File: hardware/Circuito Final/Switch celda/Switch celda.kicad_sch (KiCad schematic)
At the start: 17 parts, among them Q1 MMBT2222A, Q2 MMBT2907A, Q3 MMBT2222A

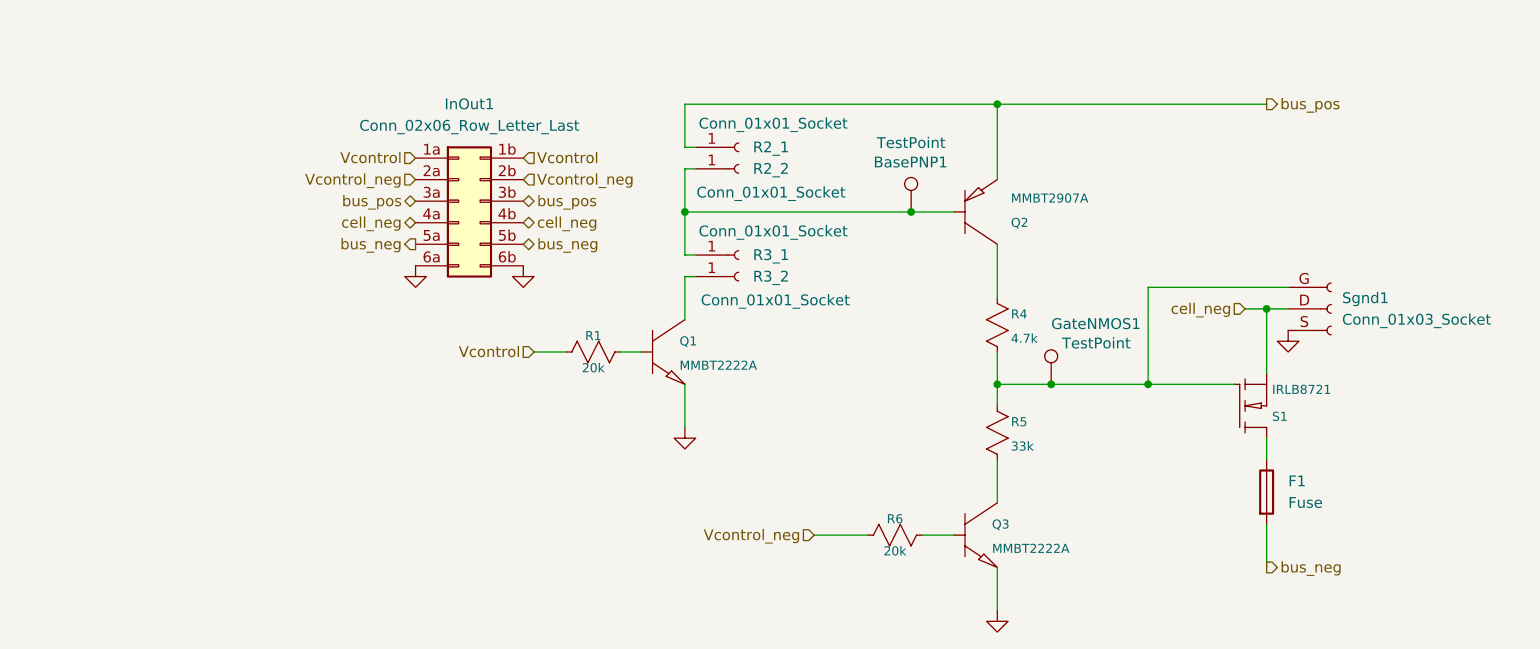
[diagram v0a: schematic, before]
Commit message: Proyecto de la celda corregido
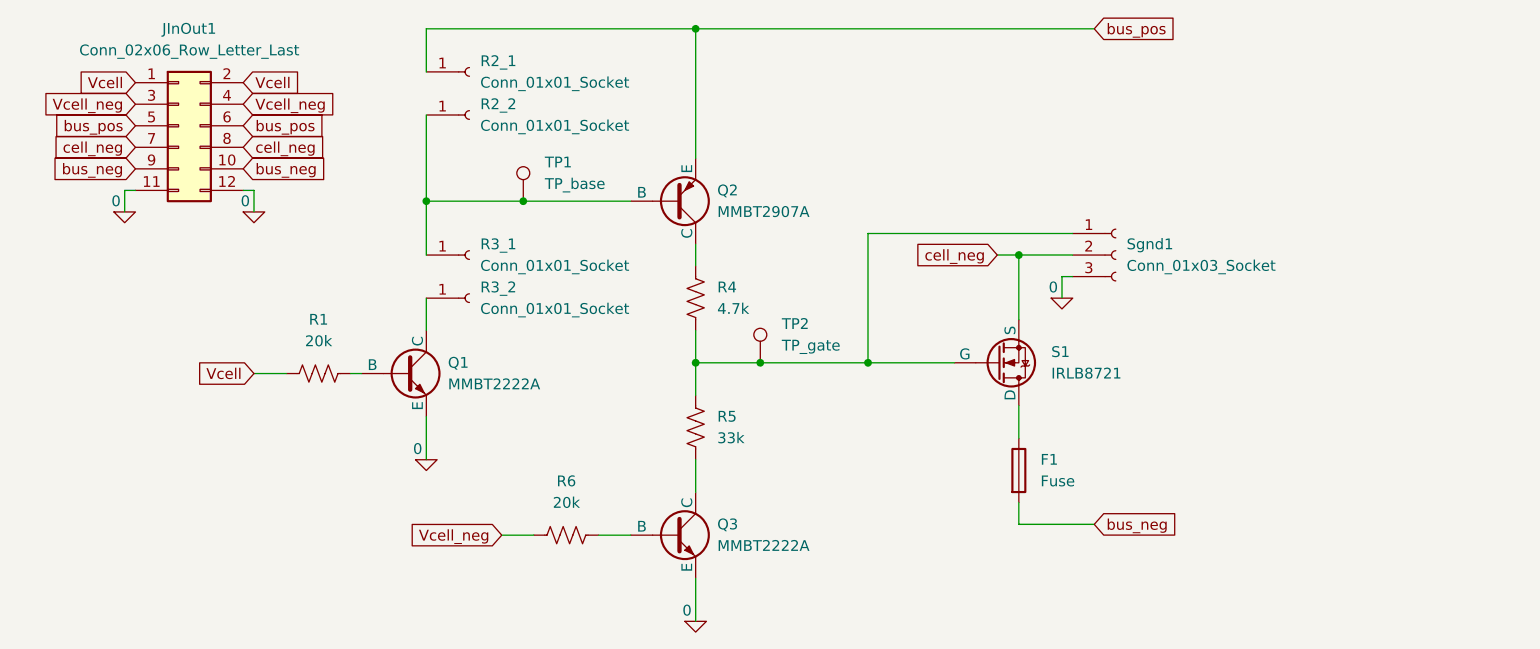
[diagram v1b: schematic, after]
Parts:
- removed BasePNP1, GateNMOS1: TestPoint, TestPoint:TestPoint_Bridge_Pitch2.54mm_Drill1.0mm, symbol Connector:TestPoint
- removed InOut1: Conn_02x06_Row_Letter_Last, Connector_PinHeader_2.54mm:PinHeader_2x06_P2.54mm_Vertical, symbol Connector_Generic:Conn_02x06_Row_Letter_Last
- removed Q1, Q3: MMBT2222A, Package_TO_SOT_SMD:SOT-23-3, symbol modificados:npn
- removed Q2: MMBT2907A, Package_TO_SOT_SMD:SOT-23-3, symbol modificados:pnp
- removed R1, R6: 20k, Resistor_THT:R_Axial_DIN0207_L6.3mm_D2.5mm_P7.62mm_Horizontal, symbol ltspice:res
- removed R4: 4.7k, Resistor_THT:R_Axial_DIN0207_L6.3mm_D2.5mm_P7.62mm_Horizontal, symbol ltspice:res
- removed R5: 33k, Resistor_THT:R_Axial_DIN0207_L6.3mm_D2.5mm_P7.62mm_Horizontal, symbol ltspice:res
- removed S1: IRLB8721, Package_TO_SOT_THT:TO-220-3_Vertical, symbol modificados:nmos
- added JInOut1: Conn_02x06_Row_Letter_Last, Connector_PinHeader_2.54mm:PinHeader_2x06_P2.54mm_Horizontal, symbol Connector_Generic:Conn_02x06_Row_Letter_Last
- added Q1, Q3: MMBT2222A, Package_TO_SOT_SMD:SOT-23-3, symbol Simulation_SPICE:NPN
- added Q2: MMBT2907A, Package_TO_SOT_SMD:SOT-23-3, symbol Simulation_SPICE:PNP
- added R1, R6: 20k, Resistor_SMD:R_0603_1608Metric_Pad0.98x0.95mm_HandSolder, symbol Device:R_US
- added R4: 4.7k, Resistor_SMD:R_0603_1608Metric_Pad0.98x0.95mm_HandSolder, symbol Device:R_US
- added R5: 33k, Resistor_SMD:R_0603_1608Metric_Pad0.98x0.95mm_HandSolder, symbol Device:R_US
- added S1: IRLB8721, Package_TO_SOT_THT:TO-220-3_Vertical, symbol Simulation_SPICE:NMOS
- added TP1: TP_base, TestPoint:TestPoint_Bridge_Pitch2.54mm_Drill1.0mm, symbol Connector:TestPoint
- added TP2: TP_gate, TestPoint:TestPoint_Bridge_Pitch2.54mm_Drill1.0mm, symbol Connector:TestPoint
- F1: footprint Huellas:Fuseholder_Cylinder-5x20mm_Schurter_0031_8201_Horizontal_Open -> Resistor_SMD:R_0603_1608Metric_Pad0.98x0.95mm_HandSolder
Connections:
- net 0: now also Sgnd1.3 (Pin_3), JInOut1.11 (Pin_6a), JInOut1.12 (Pin_6b), Q1.3 (E), Q3.3 (E); no longer Sgnd1.S (Pin_3)
- net bus_neg: now also JInOut1.10 (Pin_5b), JInOut1.9 (Pin_5a)
- net bus_pos: now also JInOut1.5 (Pin_3a), JInOut1.6 (Pin_3b), Q2.3 (E)
- net cell_neg: now also Sgnd1.2 (Pin_2), JInOut1.7 (Pin_4a), JInOut1.8 (Pin_4b), S1.3 (S); no longer Sgnd1.D (Pin_2)
- net at F1.1: now also S1.1 (D)
- net at R2_2.1 (Pin_1), R3_1.1 (Pin_1): now also Q2.2 (B), TP1.1
- net at R3_2.1 (Pin_1): now also Q1.1 (C)
- new net: R4.1, R5.2, S1.2 (G), Sgnd1.1 (Pin_1), TP2.1
- new net: Q3.1 (C), R5.1
- new net: Q3.2 (B), R6.2
- new net: Q1.2 (B), R1.2
- new net: Q2.1 (C), R4.2
- new net Vcell: JInOut1.1 (Pin_1a), JInOut1.2 (Pin_1b), R1.1
- new net Vcell_neg: JInOut1.3 (Pin_2a), JInOut1.4 (Pin_2b), R6.1

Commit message: sube mediciones y comentarios de kicad
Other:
- note added: "agregar LED agregar micro ATtiny agregar inversor MOS? volar Vcell_neg y agregar Vcc (todas compartidas salvo cell_neg) topologia torrecita por banco"
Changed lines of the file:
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@@
+		)
+	)
+	(text "agregar LED\nagregar micro ATtiny\nagregar inversor MOS?\nvolar Vcell_neg y agregar Vcc (todas compartidas salvo cell_neg)\ntopologia torrecita por banco\n"
+		(exclude_from_sim no)
+		(at 48.26 115.062 0)
+		(effects
+			(font
+				(size 1.27 1.27)
+			)
 		)
 	)

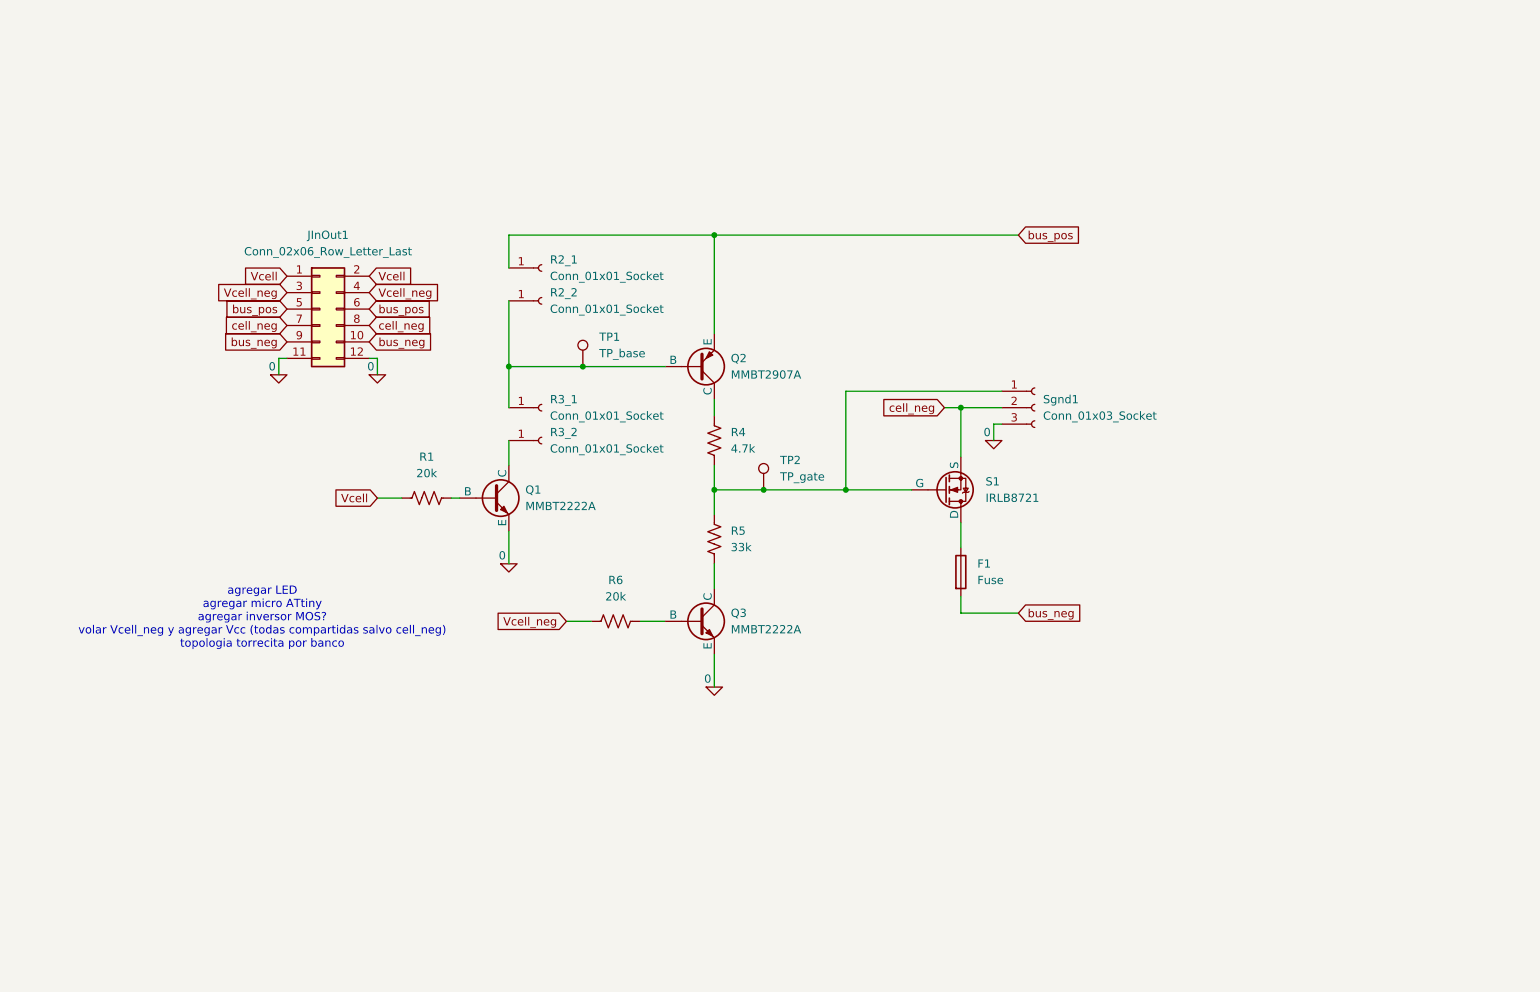
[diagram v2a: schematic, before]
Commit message: Actualización del esqumático del circuito de las celdas
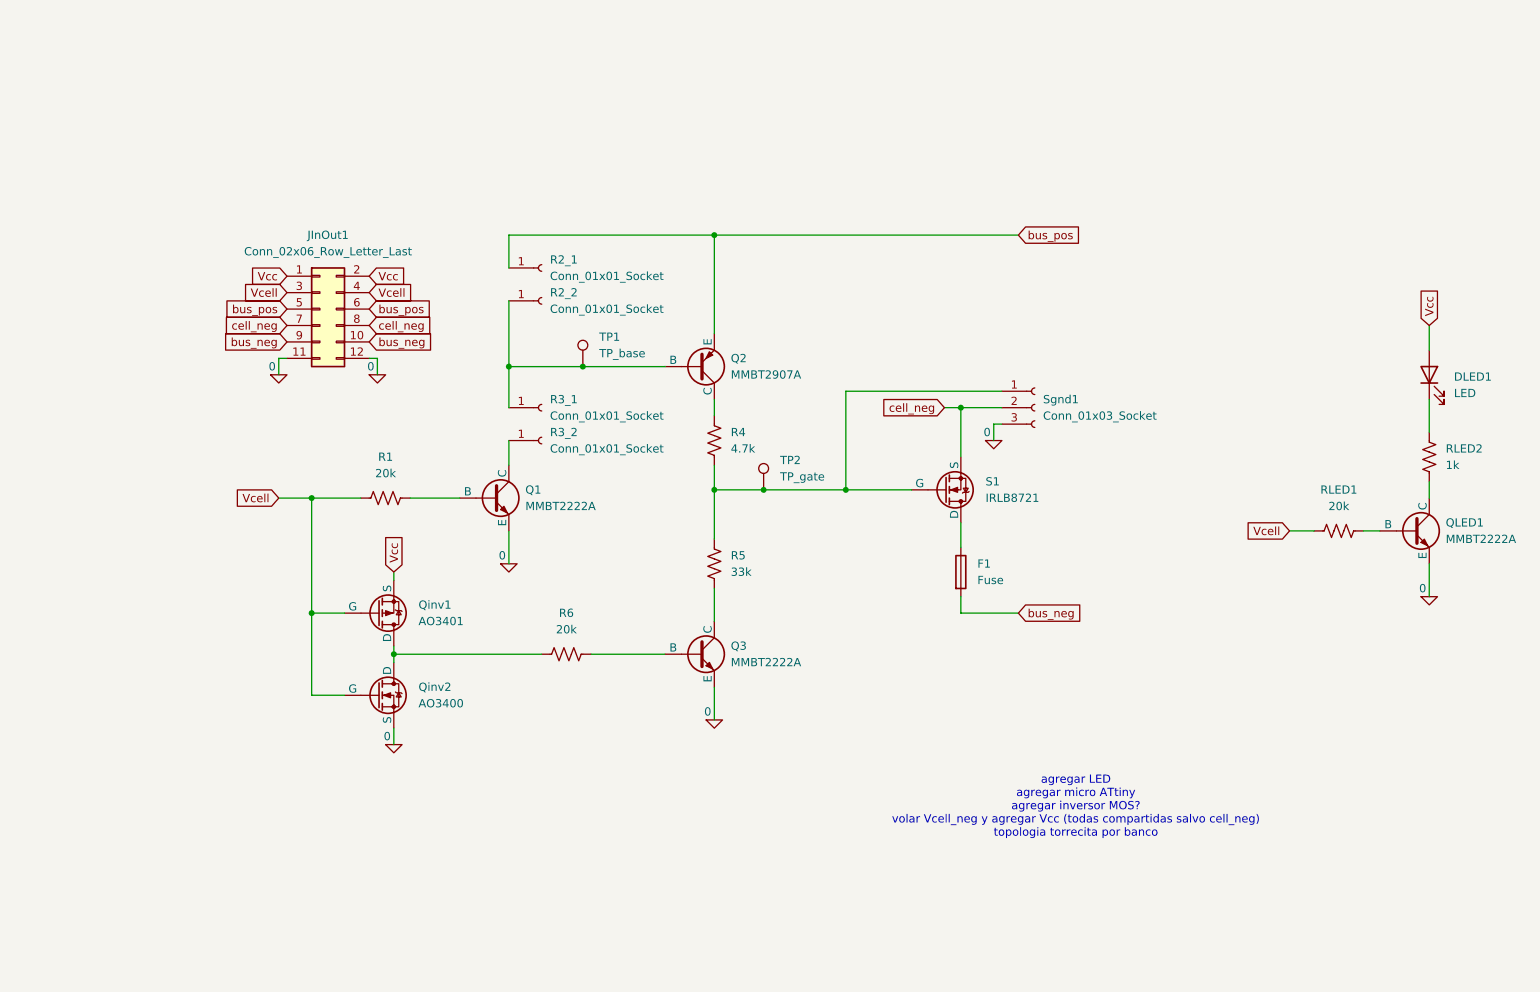
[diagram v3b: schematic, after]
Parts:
- added DLED1: LED, symbol Device:LED
- added QLED1: MMBT2222A, Package_TO_SOT_SMD:SOT-23-3, symbol Simulation_SPICE:NPN
- added Qinv1: AO3401, symbol Simulation_SPICE:PMOS
- added Qinv2: AO3400, symbol Simulation_SPICE:NMOS
- added RLED1: 20k, Resistor_SMD:R_0603_1608Metric_Pad0.98x0.95mm_HandSolder, symbol Device:R_US
- added RLED2: 1k, Resistor_SMD:R_0603_1608Metric_Pad0.98x0.95mm_HandSolder, symbol Device:R_US
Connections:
- net 0: now also QLED1.3 (E), Qinv2.3 (S)
- net Vcell: now also JInOut1.3 (Pin_2a), JInOut1.4 (Pin_2b), Qinv1.2 (G), Qinv2.2 (G), RLED1.1; no longer JInOut1.1 (Pin_1a), JInOut1.2 (Pin_1b)
- removed net Vcell_neg: JInOut1.3 (Pin_2a), JInOut1.4 (Pin_2b), R6.1
- new net: Qinv1.1 (D), Qinv2.1 (D), R6.1
- new net: QLED1.2 (B), RLED1.2
- new net: QLED1.1 (C), RLED2.1
- new net: DLED1.1 (K), RLED2.2
- new net Vcc: DLED1.2 (A), JInOut1.1 (Pin_1a), JInOut1.2 (Pin_1b), Qinv1.3 (S)
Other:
- moved on the sheet: Q3, R1, R5, R6

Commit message: Se elimina el fusible del circuito del switch de las celdas
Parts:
- removed F1: Fuse, Resistor_SMD:R_0603_1608Metric_Pad0.98x0.95mm_HandSolder, symbol Device:Fuse
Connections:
- net bus_neg: now also S1.1 (D)
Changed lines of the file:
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@@
 	(generator_version "9.0")
 	(paper "A4")
-		(symbol "Device:Fuse"
-			(pin_numbers
-				(hide yes)
-			)
-			(pin_names
-				(offset 0)
-			)
-			(exclude_from_sim no)
-			(in_bom yes)
-			(on_board yes)
-			(property "Reference" "F"
-				(at 2.032 0 90)
-				(effects
-					(font
-						(size 1.27 1.27)
-					)
-				)
-			)
-			(property "Value" "Fuse"
-				(at -1.905 0 90)
-				(effects
-					(font
-						(size 1.27 1.27)
-					)
-				)
-			)
-			(property "Footprint" ""
-				(at -1.778 0 90)
-				(effects
-					(font
-						(size 1.27 1.27)
-					)
-					(hide yes)
-				)
-			)
-			(property "Datasheet" "~"
-				(at 0 0 0)
-				(effects
-					(font
-						(size 1.27 1.27)
-					)
-					(hide yes)
-				)
-			)
-			(property "Description" "Fuse"
-				(at 0 0 0)
-				(effects
-					(font
-						(size 1.27 1.27)
-					)
-					(hide yes)
-				)
-			)
-			(property "ki_keywords" "fuse"
-				(at 0 0 0)
-				(effects
-					(font
-						(size 1.27 1.27)
-					)
-					(hide yes)
-				)
-			)
-			(property "ki_fp_filters" "*Fuse*"
-				(at 0 0 0)
-				(effects
-					(font
-						(size 1.27 1.27)
-					)
-					(hide yes)
-				)
-			)
-			(symbol "Fuse_0_1"
-				(rectangle
-					(start -0.762 -2.54)
-					(end 0.762 2.54)
-					(stroke
-						(width 0.254)
-						(type default)
-					)
-					(fill
-						(type none)
-					)
-				)
-				(polyline
-					(pts
-						(xy 0 2.54) (xy 0 -2.54)
-					)
-					(stroke
-						(width 0)
-						(type default)
-					)
-					(fill
-						(type none)
-					)
-				)
-			)
-			(symbol "Fuse_1_1"
-				(pin passive line
-					(at 0 3.81 270)
-					(length 1.27)
-					(name "~"
-						(effects
-							(font
-								(size 1.27 1.27)
-							)
-						)
-					)
-					(number "1"
-						(effects
-							(font
-								(size 1.27 1.27)
-							)
-						)
-					)
-				)
-				(pin passive line
-					(at 0 -3.81 90)
-					(length 1.27)
-					(name "~"
-						(effects
-							(font
-								(size 1.27 1.27)
-							)
-						)
-					)
-					(number "2"
-						(effects
-							(font
-								(size 1.27 1.27)
-							)
-						)
-					)
-				)
-			)
-			(embedded_fonts no)
-		)
 		(symbol "Device:LED"
 			(pin_numbers
@@
 	(wire
 		(pts
-			(xy 156.21 100.33) (xy 156.21 104.14)
-		)
-		(stroke
-			(width 0)
-			(type default)
-		)
-	)
-	(wire
-		(pts
 			(xy 161.29 85.09) (xy 161.29 87.63)
 		)
@@
 	(wire
 		(pts
-			(xy 156.21 114.3) (xy 165.1 114.3)
-		)
-		(stroke
-			(width 0)
-			(type default)
-		)
-	)
-	(wire
-		(pts
 			(xy 228.6 106.68) (xy 228.6 111.76)
 		)
@@
 	(wire
 		(pts
-			(xy 156.21 111.76) (xy 156.21 114.3)
+			(xy 156.21 100.33) (xy 156.21 106.68)
 		)
 		(stroke
@@
 	(global_label "bus_neg"
 		(shape input)
-		(at 165.1 114.3 0)
+		(at 156.21 106.68 270)
 		(fields_autoplaced yes)
 		(effects
@@
 				(size 1.27 1.27)
 			)
-			(justify left)
+			(justify right)
 		)
 		(property "Intersheetrefs" "${INTERSHEET_REFS}"
-			(at 175.7655 114.3 0)
+			(at 156.21 117.3455 90)
 			(effects
 				(font
 					(size 1.27 1.27)
 				)
-				(justify left)
+				(justify right)
 				(hide yes)
 			)
@@
 					(unit 1)
 				)
-			)
-		)
-	)
-	(symbol
-		(lib_id "Device:Fuse")
-		(at 156.21 107.95 0)
-		(unit 1)
-		(exclude_from_sim no)
-		(in_bom yes)
-		(on_board yes)
-		(dnp no)
-		(fields_autoplaced yes)
-		(property "Reference" "F1"
-			(at 158.75 106.6799 0)
-			(effects
-				(font
-					(size 1.27 1.27)
-				)
-				(justify left)
-			)
-		)
-		(property "Value" "Fuse"
-			(at 158.75 109.2199 0)
-			(effects
-				(font
-					(size 1.27 1.27)
-				)
-				(justify left)
-			)
-		)
-		(property "Footprint" "Resistor_SMD:R_0603_1608Metric_Pad0.98x0.95mm_HandSolder"
-			(at 154.432 107.95 90)
-			(effects
-				(font
-					(size 1.27 1.27)
-				)
-				(hide yes)
-			)
-		)
-		(property "Datasheet" "~"
-			(at 156.21 107.95 0)
-			(effects
-				(font
-					(size 1.27 1.27)
-				)
-				(hide yes)
-			)
-		)
-		(property "Description" "Fuse"
-			(at 156.21 107.95 0)
-			(effects
-				(font
-					(size 1.27 1.27)
-				)
-				(hide yes)
-			)
-		)
-		(pin "2"
-		)
-		(pin "1"
-		)
-		(instances
-			(project ""
-				(path "/4783565b-68b0-4d0c-b0f9-91a8fe34107e"
-					(reference "F1")
-					(unit 1)
-				)

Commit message: update pcb
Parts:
- removed JInOut1: Conn_02x06_Row_Letter_Last, Connector_PinHeader_2.54mm:PinHeader_2x06_P2.54mm_Horizontal, symbol Connector_Generic:Conn_02x06_Row_Letter_Last
- added Celda1: Portapilas 18650, symbol Device:Battery_Cell
- added JInOut1, JInOut2: Conn_02x05_Odd_Even, symbol Connector_Generic:Conn_02x05_Odd_Even
- added TP3: TP_inv, TestPoint:TestPoint_Bridge_Pitch2.54mm_Drill1.0mm, symbol Connector:TestPoint
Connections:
- net 0: now also JInOut1.10 (Pin_10), JInOut1.9 (Pin_9), JInOut2.10 (Pin_10), JInOut2.9 (Pin_9)
- net Vcc: now also JInOut1.1 (Pin_1), JInOut1.2 (Pin_2), JInOut2.1 (Pin_1), JInOut2.2 (Pin_2)
- net Vcell: now also JInOut1.3 (Pin_3), JInOut1.4 (Pin_4), JInOut2.3 (Pin_3), JInOut2.4 (Pin_4)
- net bus_neg: now also JInOut1.7 (Pin_7), JInOut1.8 (Pin_8), JInOut2.7 (Pin_7), JInOut2.8 (Pin_8)
- net bus_pos: now also Celda1.1 (+), JInOut1.5 (Pin_5), JInOut1.6 (Pin_6), JInOut2.5 (Pin_5), JInOut2.6 (Pin_6)
- net at Qinv1.1 (D), Qinv2.1 (D), R6.1: now also TP3.1
- net cell_neg: no longer names the net of S1.3 (S), Sgnd1.2 (Pin_2)
- net cell_neg: now also Celda1.2 (-)
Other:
- moved on the sheet: R6
